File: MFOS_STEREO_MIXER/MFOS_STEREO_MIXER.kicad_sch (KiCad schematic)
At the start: 155 parts, among them J1 Barrel_Jack, J10 Barrel_Jack, J11 Barrel_Jack, J12 Barrel_Jack, J13 Barrel_Jack, J14 Barrel_Jack, J15 Barrel_Jack, J16 Barrel_Jack, J17 AudioJack2_Ground, J18 Barrel_Jack, J19 Barrel_Jack, J2 Barrel_Jack, J3 Barrel_Jack, J4 Barrel_Jack, J5 Barrel_Jack, J6 Barrel_Jack, J7 Barrel_Jack, J8 Barrel_Jack, J9 Barrel_Jack, U1 TL071, U2 TL071, U3 TL071, U4 TL071, U5 TL072, U6 TL072, U7 TL072, U8 LM386, U9 LM386

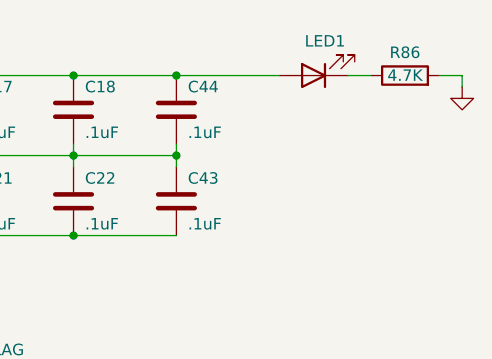
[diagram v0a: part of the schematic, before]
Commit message: Updated BOM, renamed VCO > MFOS_VCO
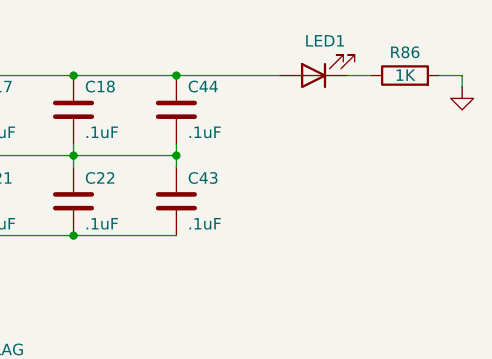
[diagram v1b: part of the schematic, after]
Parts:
- R86: value 4.7K -> 1K
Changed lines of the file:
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@@
     (in_bom yes) (on_board yes)
     (property "Reference" "R86" (id 0) (at 340.36 26.67 90))
-    (property "Value" "4.7K" (id 1) (at 340.36 29.21 90))
+    (property "Value" "1K" (id 1) (at 340.36 29.21 90))
     (property "Footprint" "" (id 2) (at 340.36 30.988 90)
       (effects (font (size 1.27 1.27)) hide)
@@
     )
     (path "/88c16a83-b8c4-4b18-a071-abb16b4db9b4"
-      (reference "R86") (unit 1) (value "4.7K") (footprint "")
+      (reference "R86") (unit 1) (value "1K") (footprint "")
     )
     (path "/7a17b386-e13f-463b-81e7-b4a3f9a8820f"

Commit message: Reviewed BOM
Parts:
- J1, J10, J11, J12, J13, J14, J15, J16, J18, J19, J2, J3, J4, J5, J6, J7, J8, J9: symbol Connector:Barrel_Jack -> Connector:Jack-DC
- R13, R17, R2, R24, R28, R32, R39, R43, R47, R54, R58, R9: symbol Device:R_Potentiometer -> dhk:R_Potentiometer_Audio_Taper
- R63, R65, R70, R72, R76: symbol Device:R_Potentiometer_Dual -> dhk:R_Potentiometer_Dual_Audio_Taper

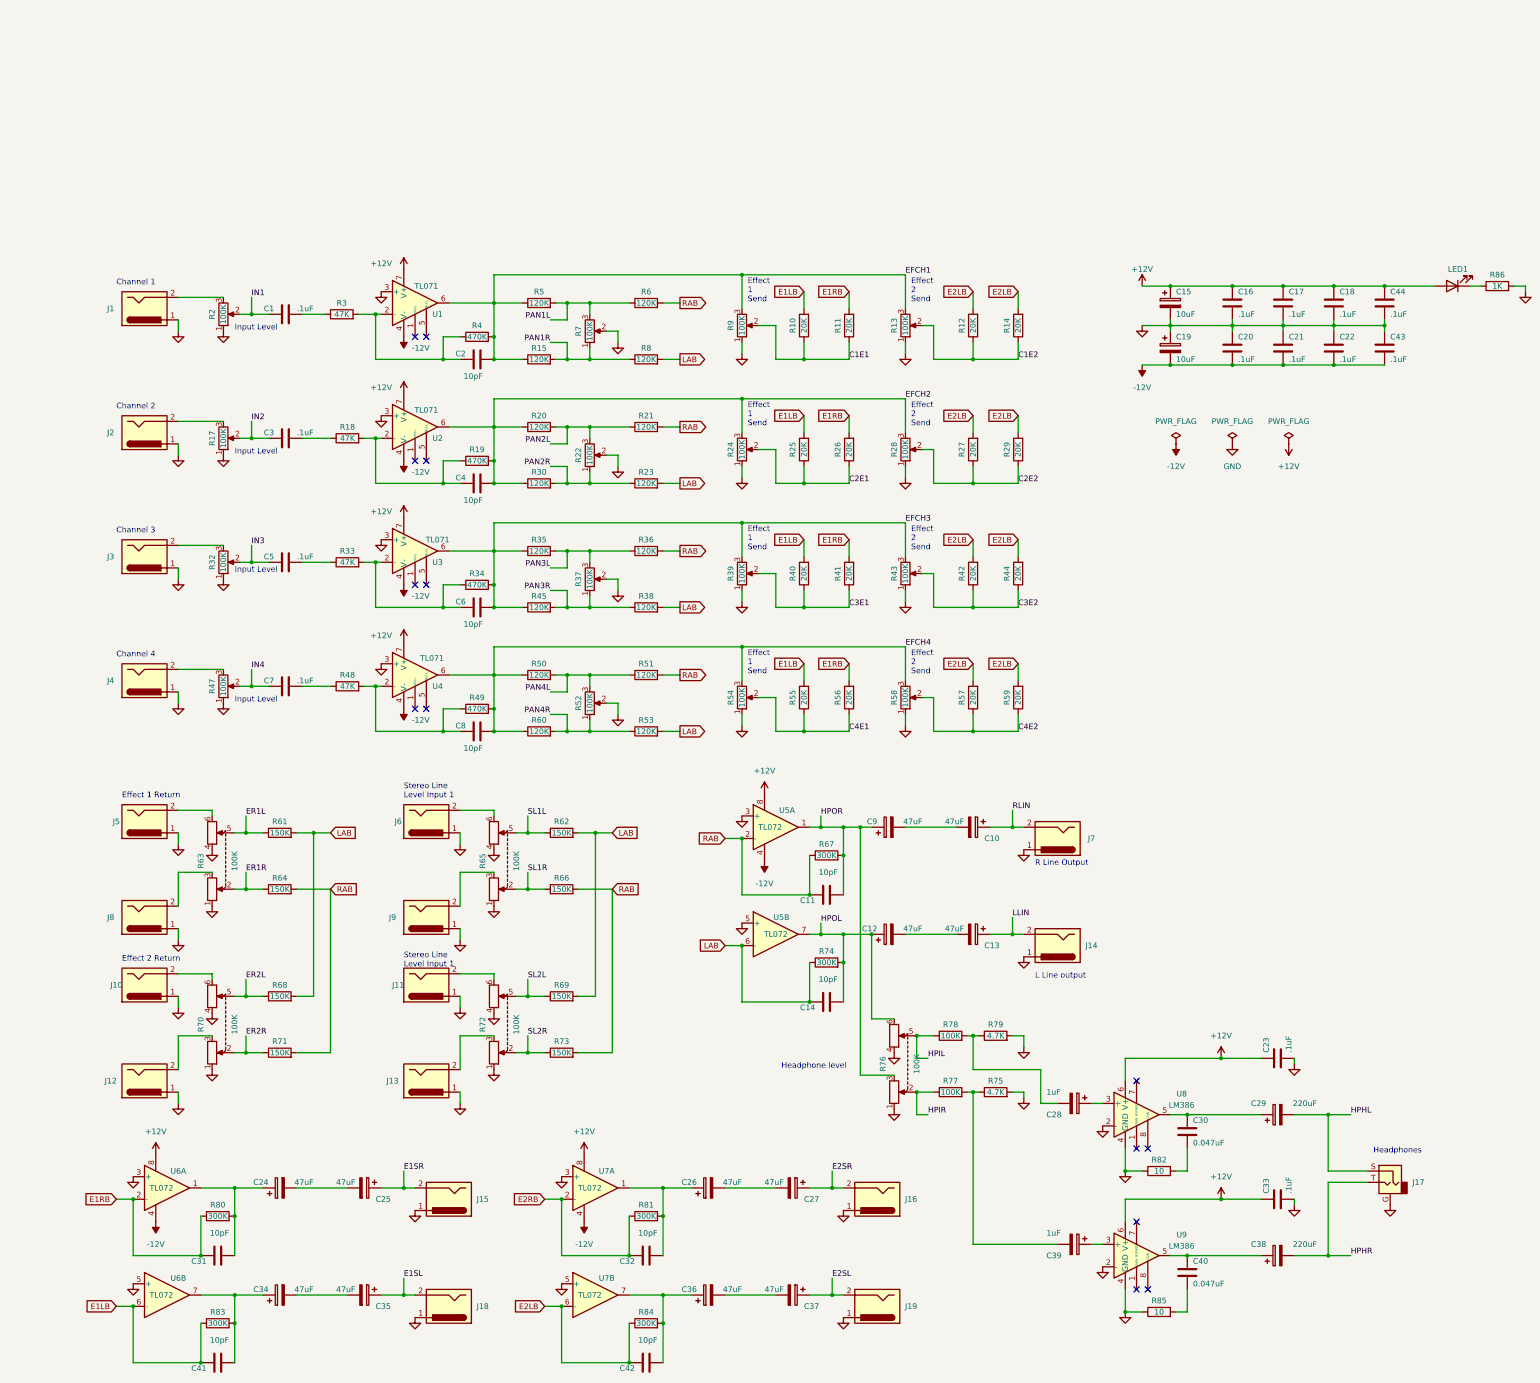
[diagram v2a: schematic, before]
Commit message: Designs adapted for BOM
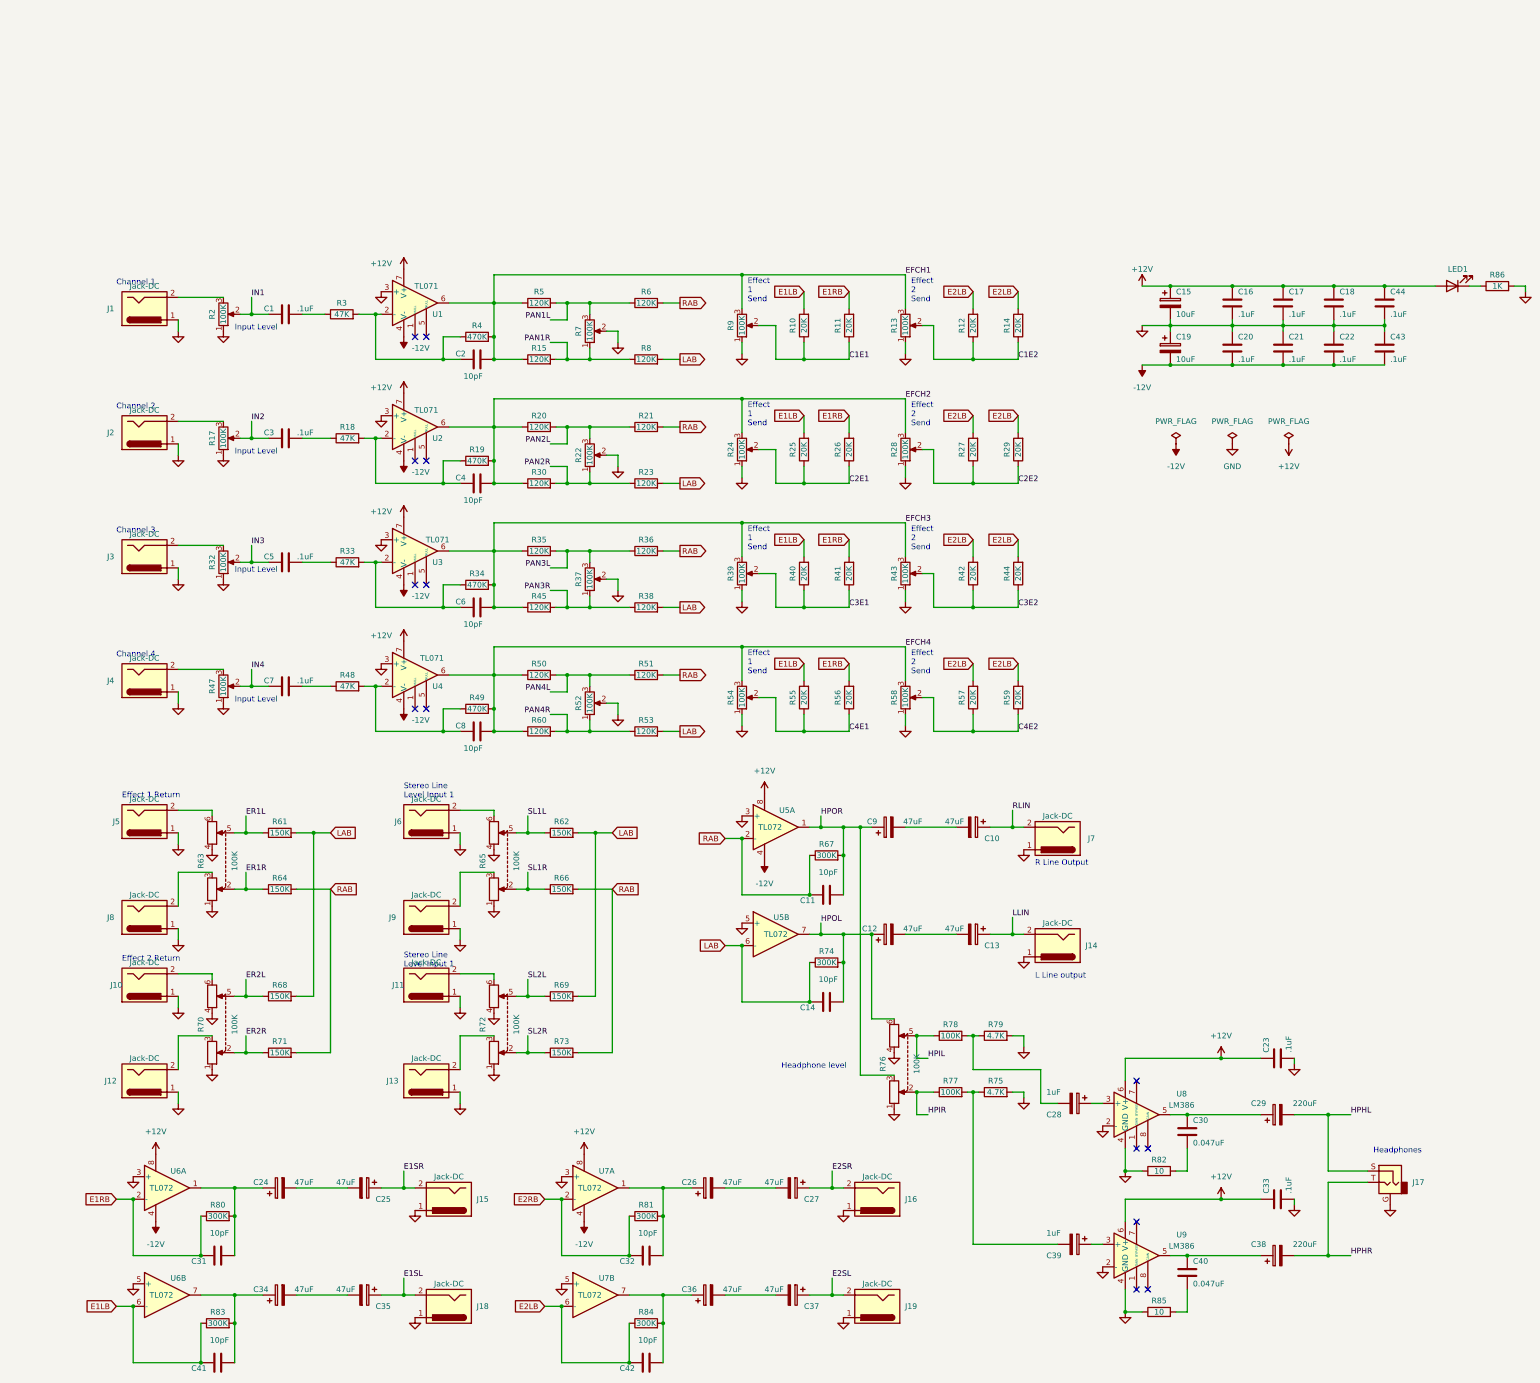
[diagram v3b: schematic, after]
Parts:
- J1, J10, J11, J12, J13, J14, J15, J16, J18, J19, J2, J3, J4, J5, J6, J7, J8, J9: value Barrel_Jack -> Jack-DC

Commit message: yeah yeah
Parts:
- removed C1, C16, C17, C18, C20, C21, C22, C23, C3, C33, C43, C44, C5, C7: .1uF, symbol Device:C
- removed C10, C12, C13, C24, C25, C26, C27, C34, C35, C36, C37, C9: 47uF, symbol Device:C_Polarized
- removed C11, C14, C2, C31, C32, C4, C41, C42, C6, C8: 10pF, symbol Device:C
- removed C15, C19: 10uF, symbol Device:C_Polarized
- removed C28, C39: 1uF, symbol Device:C_Polarized
- removed C29, C38: 220uF, symbol Device:C_Polarized
- removed C30, C40: 0.047uF, symbol Device:C
- removed J1, J10, J11, J12, J13, J14, J15, J16, J18, J19, J2, J3, J4, J5, J6, J7, J8, J9: Jack-DC, symbol Connector:Jack-DC
- removed J17: AudioJack2_Ground, symbol Connector:AudioJack2_Ground
- removed LED1: LED, symbol Device:LED
- removed R10, R11, R12, R14, R25, R26, R27, R29, R40, R41, R42, R44, R55, R56, R57, R59: 20K, symbol Device:R
- removed R13, R17, R2, R24, R28, R32, R39, R43, R47, R54, R58, R9: 100K, symbol dhk:R_Potentiometer_Audio_Taper
- removed R15, R20, R21, R23, R30, R35, R36, R38, R45, R5, R50, R51, R53, R6, R60, R8: 120K, symbol Device:R
- removed R18, R3, R33, R48: 47K, symbol Device:R
- removed R19, R34, R4, R49: 470K, symbol Device:R
- removed R22, R37, R52, R7: 100K, symbol Device:R_Potentiometer
- removed R61, R62, R64, R66, R68, R69, R71, R73: 150K, symbol Device:R
- removed R63, R65, R70, R72, R76: 100K, symbol dhk:R_Potentiometer_Dual_Audio_Taper
- removed R67, R74, R80, R81, R83, R84: 300K, symbol Device:R
- removed R75, R79: 4.7K, symbol Device:R
- removed R77, R78: 100K, symbol Device:R
- removed R82, R85: 10, symbol Device:R
- removed R86: 1K, symbol Device:R
- removed U1, U2, U3, U4: TL071, symbol Amplifier_Operational:TL071
- removed U5, U6, U7: TL072, symbol Amplifier_Operational:TL072
- removed U8, U9: LM386, symbol Amplifier_Audio:LM386
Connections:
- no-connect marks 14 -> 0
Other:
- added sheet Sheet 1 (untitled.kicad_sch)
- added sheet Sheet 3 (sheet3.kicad_sch)
- added sheet Sheet2 (sheet2.kicad_sch)
- note removed: "Channel 1"
- note removed: "Channel 2"
- note removed: "Channel 3"
- note removed: "Channel 4"
- note removed: "Effect 1 Return"
- note removed: "Effect 1 Send"
- note removed: "Effect 2 Return"
- note removed: "Effect 2 Send"
- note removed: "Headphone level"
- note removed: "Headphones"
- note removed: "Input Level"
- note removed: "L Line output"
- note removed: "R Line Output"
- note removed: "Stereo Line Level Input 1"
